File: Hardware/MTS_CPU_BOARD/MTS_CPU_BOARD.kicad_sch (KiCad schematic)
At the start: 0 parts

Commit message: Add some connectors
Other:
- added sheet CM4 (CM4.kicad_sch)
- added sheet Ethernet (Ethernet .kicad_sch)
- added sheet STM32 (STM32.kicad_sch)
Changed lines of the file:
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@@
 	(paper "A4")
+	(sheet
+		(at 128.27 29.21)
+		(size 40.64 38.1)
+		(exclude_from_sim no)
+		(in_bom yes)
+		(on_board yes)
+		(dnp no)
+		(fields_autoplaced yes)
+		(stroke
+			(width 0.1524)
+			(type solid)
+		)
+		(fill
+			(color 0 0 0 0.0000)
+		)
+		(property "Sheetname" "CM4"
+			(at 128.27 28.4984 0)
+			(effects
+				(font
+					(size 1.27 1.27)
+				)
+				(justify left bottom)
+			)
+		)
+		(property "Sheetfile" "CM4.kicad_sch"
+			(at 128.27 67.8946 0)
+			(effects
+				(font
+					(size 1.27 1.27)
+				)
+				(justify left top)
+			)
+		)
+		(instances
+			(project "MTS_CPU_BOARD"
+				(path "/b6a2ab1c-6000-4ee5-8a59-5a2d20d16b67"
+					(page "4")
+				)
+			)
+		)
+	)
 	(sheet
 		(at 29.21 27.94)
@@
 				)
 			)
+		)
+	)
+	(sheet
+		(at 72.39 29.21)
+		(size 39.37 38.1)
+		(exclude_from_sim no)
+		(in_bom yes)
+		(on_board yes)
+		(dnp no)
+		(fields_autoplaced yes)
+		(stroke
+			(width 0.1524)
+			(type solid)
+		)
+		(fill
+			(color 0 0 0 0.0000)
+		)
+		(property "Sheetname" "STM32"
+			(at 72.39 28.4984 0)
+			(effects
+				(font
+					(size 1.27 1.27)
+				)
+				(justify left bottom)
+			)
+		)
+		(property "Sheetfile" "STM32.kicad_sch"
+			(at 72.39 67.8946 0)
+			(effects
+				(font
+					(size 1.27 1.27)
+				)
+				(justify left top)
+			)
+		)
+		(instances
+			(project "MTS_CPU_BOARD"
+				(path "/b6a2ab1c-6000-4ee5-8a59-5a2d20d16b67"
+					(page "3")
+				)
+			)
+		)
+	)
+	(sheet
+		(at 179.07 29.21)
+		(size 34.29 39.37)
+		(exclude_from_sim no)
+		(in_bom yes)
+		(on_board yes)
+		(dnp no)
+		(fields_autoplaced yes)
+		(stroke
+			(width 0.1524)
+			(type solid)
+		)
+		(fill
+			(color 0 0 0 0.0000)
+		)
+		(property "Sheetname" "Ethernet"
+			(at 179.07 28.4984 0)
+			(effects
+				(font
+					(size 1.27 1.27)
+				)
+				(justify left bottom)
+			)
+		)
+		(property "Sheetfile" "Ethernet .kicad_sch"
+			(at 179.07 69.1646 0)
+			(effects
+				(font
+					(size 1.27 1.27)
+				)
+				(justify left top)
+			)
+		)
+		(instances
+			(project "MTS_CPU_BOARD"
+				(path "/b6a2ab1c-6000-4ee5-8a59-5a2d20d16b67"
+					(page "5")
+				)
+			)

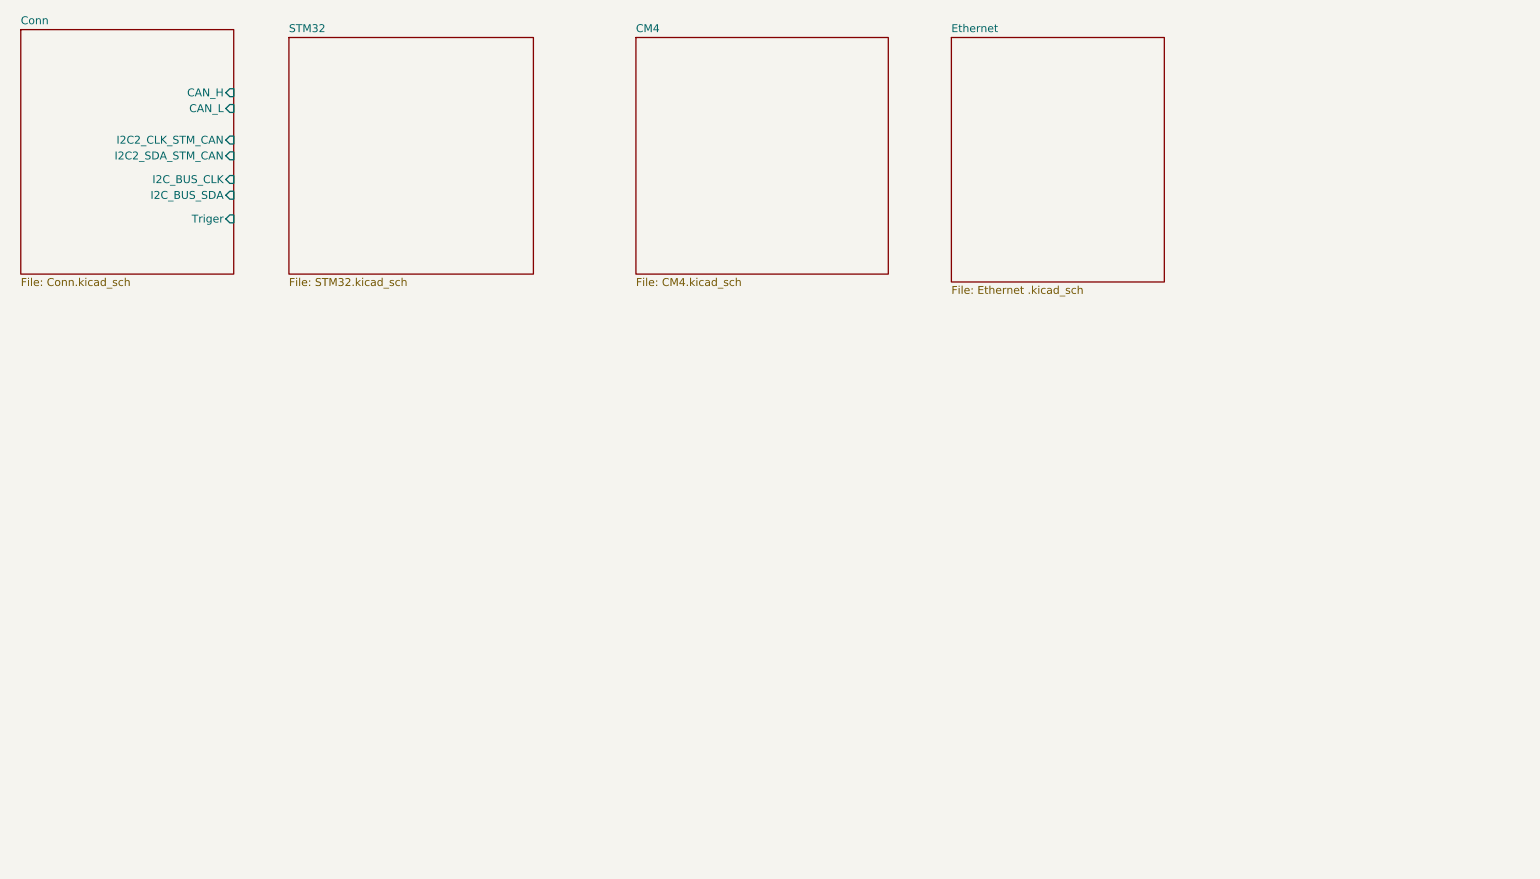
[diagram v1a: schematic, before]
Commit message: Add EtherCAT
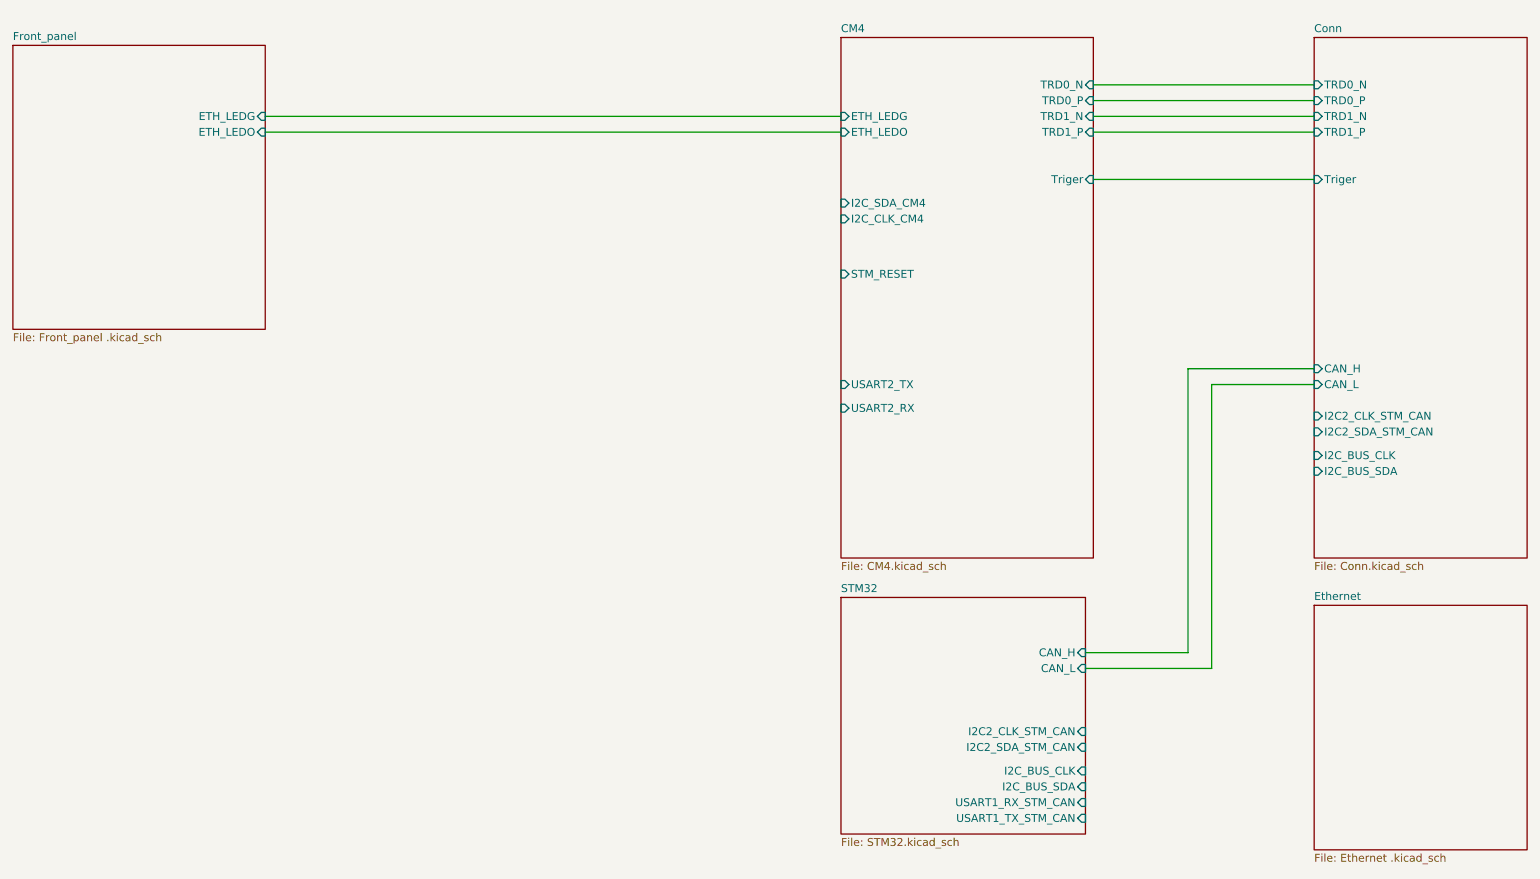
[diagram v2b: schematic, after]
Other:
- added sheet Front_panel (Front_panel .kicad_sch)
- sheet CM4 ports: added ETH_LEDG, ETH_LEDO, I2C_CLK_CM4, I2C_SDA_CM4, STM_RESET, TRD0_N, TRD0_P, TRD1_N, TRD1_P, Triger, USART2_RX, USART2_TX; removed none
- sheet Conn ports: added TRD0_N, TRD0_P, TRD1_N, TRD1_P; removed none
- sheet STM32 ports: added CAN_H, CAN_L, I2C2_CLK_STM_CAN, I2C2_SDA_STM_CAN, I2C_BUS_CLK, I2C_BUS_SDA, USART1_RX_STM_CAN, USART1_TX_STM_CAN; removed none

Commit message: Add status Led´s
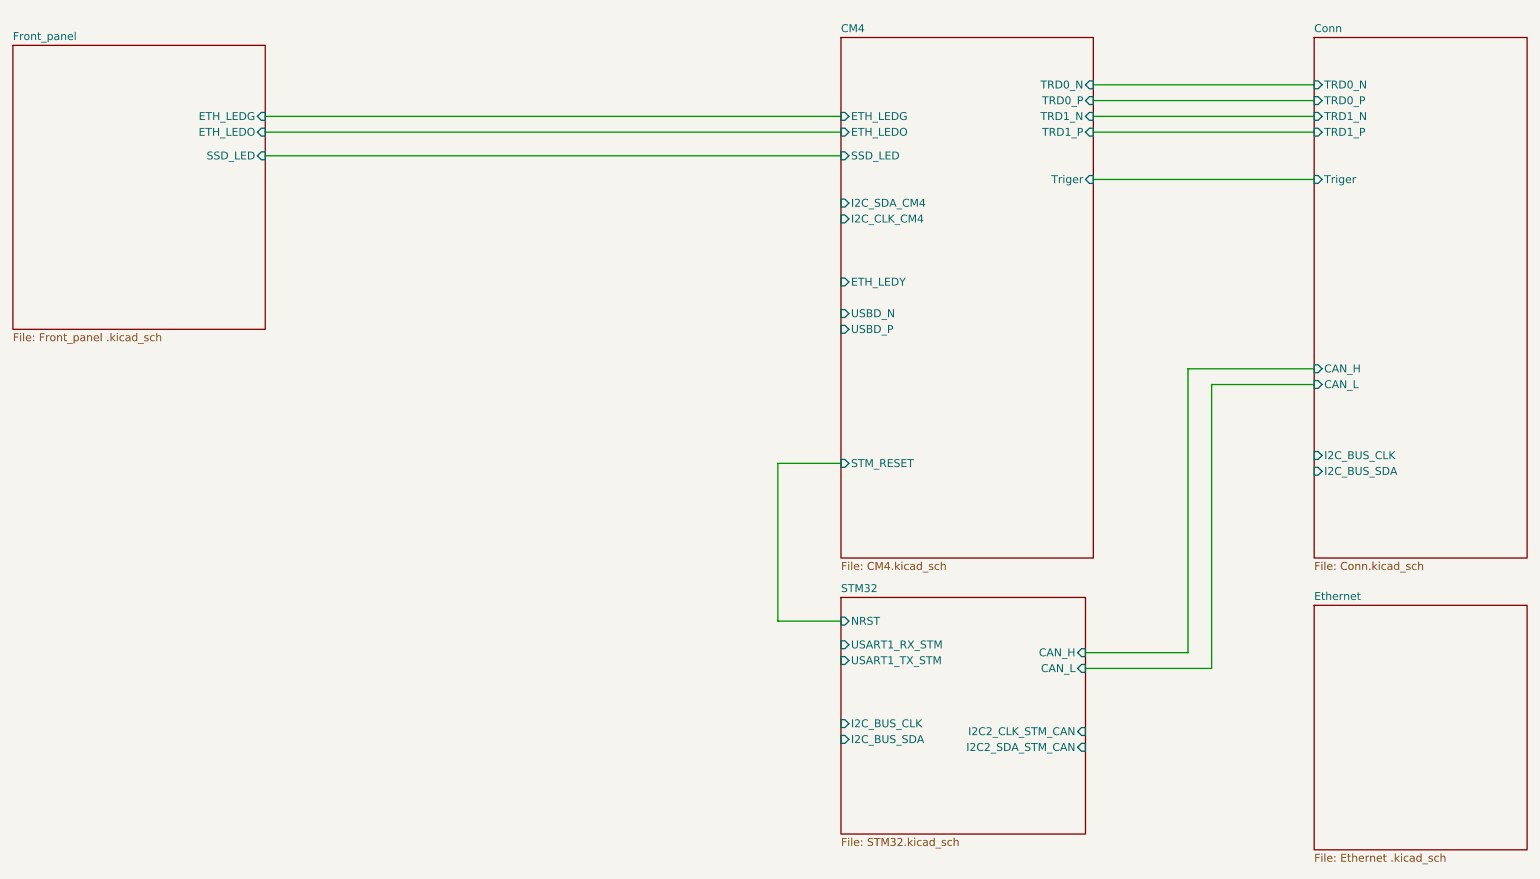
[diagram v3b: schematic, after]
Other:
- sheet CM4 ports: added ETH_LEDY, SSD_LED, USBD_N, USBD_P; removed USART2_RX, USART2_TX
- sheet Conn ports: added none; removed I2C2_CLK_STM_CAN, I2C2_SDA_STM_CAN
- sheet Front_panel ports: added SSD_LED; removed none
- sheet STM32 ports: added NRST, USART1_RX_STM, USART1_TX_STM; removed USART1_RX_STM_CAN, USART1_TX_STM_CAN
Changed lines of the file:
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@@
+	(wire
+		(pts
+			(xy 151.13 123.19) (xy 151.13 97.79)
+		)
+		(stroke
+			(width 0)
+			(type default)
+		)
+	)
 	(wire
 		(pts
@@
 	(wire
 		(pts
+			(xy 151.13 97.79) (xy 161.29 97.79)
+		)
+		(stroke
+			(width 0)
+			(type default)
+		)
+	)
+	(wire
+		(pts
 			(xy 220.98 130.81) (xy 200.66 130.81)
 		)
@@
 	(wire
 		(pts
+			(xy 161.29 123.19) (xy 151.13 123.19)
+		)
+		(stroke
+			(width 0)
+			(type default)
+		)
+	)
+	(wire
+		(pts
 			(xy 201.93 41.91) (xy 237.49 41.91)
 		)
@@
 		(pts
 			(xy 201.93 39.37) (xy 237.49 39.37)
+		)
+		(stroke
+			(width 0)
+			(type default)
+		)
+	)
+	(wire
+		(pts
+			(xy 68.58 48.26) (xy 161.29 48.26)
 		)
 		(stroke
@@
 			)
 		)
-		(pin "USART2_RX" input
-			(at 161.29 88.9 180)
-			(effects
-				(font
-					(size 1.27 1.27)
-				)
-				(justify left)
-			)
-		)
-		(pin "USART2_TX" input
-			(at 161.29 85.09 180)
-			(effects
-				(font
-					(size 1.27 1.27)
-				)
-				(justify left)
-			)
-		)
 		(pin "I2C_CLK_CM4" input
 			(at 161.29 58.42 180)
@@
 		)
 		(pin "STM_RESET" input
-			(at 161.29 67.31 180)
+			(at 161.29 97.79 180)
 			(effects
 				(font
@@
 				)
 				(justify right)
+			)
+		)
+		(pin "ETH_LEDY" input
+			(at 161.29 68.58 180)
+			(effects
+				(font
+					(size 1.27 1.27)
+				)
+				(justify left)
+			)
+		)
+		(pin "SSD_LED" input
+			(at 161.29 48.26 180)
+			(effects
+				(font
+					(size 1.27 1.27)
+				)
+				(justify left)
+			)
+		)
+		(pin "USBD_N" input
+			(at 161.29 73.66 180)
+			(effects
+				(font
+					(size 1.27 1.27)
+				)
+				(justify left)
+			)
+		)
+		(pin "USBD_P" input
+			(at 161.29 76.2 180)
+			(effects
+				(font
+					(size 1.27 1.27)
+				)
+				(justify left)
 			)
 		)
@@
 			)
 		)
+		(pin "SSD_LED" input
+			(at 68.58 48.26 0)
+			(effects
+				(font
+					(size 1.27 1.27)
+				)
+				(justify right)
+			)
+		)
 		(instances
 			(project "MTS_CPU_BOARD"
@@
 			)
 		)
-		(pin "I2C2_CLK_STM_CAN" input
-			(at 237.49 90.17 180)
-			(effects
-				(font
-					(size 1.27 1.27)
-				)
-				(justify left)
-			)
-		)
-		(pin "I2C2_SDA_STM_CAN" input
-			(at 237.49 92.71 180)
-			(effects
-				(font
-					(size 1.27 1.27)
-				)
-				(justify left)
-			)
-		)
 		(pin "I2C_BUS_CLK" input
 			(at 237.49 96.52 180)
@@
 		)
 		(pin "I2C_BUS_CLK" input
-			(at 200.66 147.32 0)
-			(effects
-				(font
-					(size 1.27 1.27)
-				)
-				(justify right)
+			(at 161.29 139.7 180)
+			(effects
+				(font
+					(size 1.27 1.27)
+				)
+				(justify left)
 			)
 		)
 		(pin "I2C_BUS_SDA" input
-			(at 200.66 149.86 0)
-			(effects
-				(font
-					(size 1.27 1.27)
-				)
-				(justify right)
-			)
-		)
-		(pin "USART1_RX_STM_CAN" input
-			(at 200.66 152.4 0)
-			(effects
-				(font
-					(size 1.27 1.27)
-				)
-				(justify right)
-			)
-		)
-		(pin "USART1_TX_STM_CAN" input
-			(at 200.66 154.94 0)
-			(effects
-				(font
-					(size 1.27 1.27)
-				)
-				(justify right)
-			)
-		)
+			(at 161.29 142.24 180)
+			(effects
+				(font
+					(size 1.27 1.27)
+				)
+				(justify left)
+			)
+		)
+		(pin "USART1_RX_STM" input
+			(at 161.29 127 180)
+			(effects
+				(font
+					(size 1.27 1.27)
+				)
+				(justify left)
+			)
+		)
+		(pin "USART1_TX_STM" input
+			(at 161.29 129.54 180)
+			(effects
+				(font
+					(size 1.27 1.27)
+				)
+				(justify left)
+			)
+		)
+		(pin "NRST" input
+			(at 161.29 123.19 180)
+			(effects
+				(font
+					(size 1.27 1.27)
+				)
+				(justify left)
+			)
+		)
